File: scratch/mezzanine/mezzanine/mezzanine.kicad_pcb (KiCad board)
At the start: 2 copper layers, 141.5 x 62.2 mm, 18 parts, among them J101 Conn_02x20_Counter_Clockwise_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, J102 Conn_02x20_Counter_Clockwise_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, J103 Conn_02x10_Odd_Even, U101 Caravel_COB, U102 Caravel_COB

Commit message: padring v0.1
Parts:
- added G***: LOGO, Symbol:waferspace_pin1, F.Cu at (207.7, 123.9)
- added G***: LOGO, Symbol:waferspace_pin1, F.Cu at (208.1, 142.3)
- added G***: LOGO, Symbol:waferspace_pin1, B.Cu at (225.1, 155.1)
- added U101: Caravel_COB, WafeSpace:waferspace_default_padring_v0, F.Cu at (214.1, 148.5)
- added U101: Caravel_COB, WafeSpace:waferspace_default_padring_v0, B.Cu at (231.5, 148.3)
- added U102: Caravel_COB, WafeSpace:caravel_gfmpw_1_0_asap, F.Cu at (153.4, 133.3)
- added U103: Caravel_COB, WafeSpace:LGA2, B.Cu at (153.4, 140.0)
- added U104: Caravel_COB, WafeSpace:LGA1, F.Cu at (231.6, 148.4)
- added U104: Caravel_COB, WafeSpace:LGA1, B.Cu at (214.2, 148.4)
- renumbered U101 to U102, U102 to U104
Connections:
- U104 pad 1: (no net) -> unconnected-(U104-mprj_io[24]-Pad1) (x2)
- U104 pad 2: (no net) -> unconnected-(U104-mprj_io[25]-Pad2) (x2)
- U104 pad 3: (no net) -> unconnected-(U104-mprj_io[26]-Pad3) (x2)
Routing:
- net (no net): track 0.00 -> 5.02 mm, vias 2 -> 5
- net unconnected-(U102-mprj_io[23]-Pad45): track 0.00 -> 3.72 mm, vias 0 -> 1
- net unconnected-(U102-mprj_io[0]_JTAG-Pad22): track 0.00 -> 2.00 mm, vias 0 -> 1
- net unconnected-(U102-mprj_io[1]_SDO-Pad23): track 0.00 -> 1.84 mm, vias 0 -> 1
- net unconnected-(U102-mprj_io[2]_SDI-Pad24): track 0.00 -> 1.64 mm, vias 0 -> 1
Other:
- board size 141.5 x 62.2 mm -> 141.5 x 80 mm

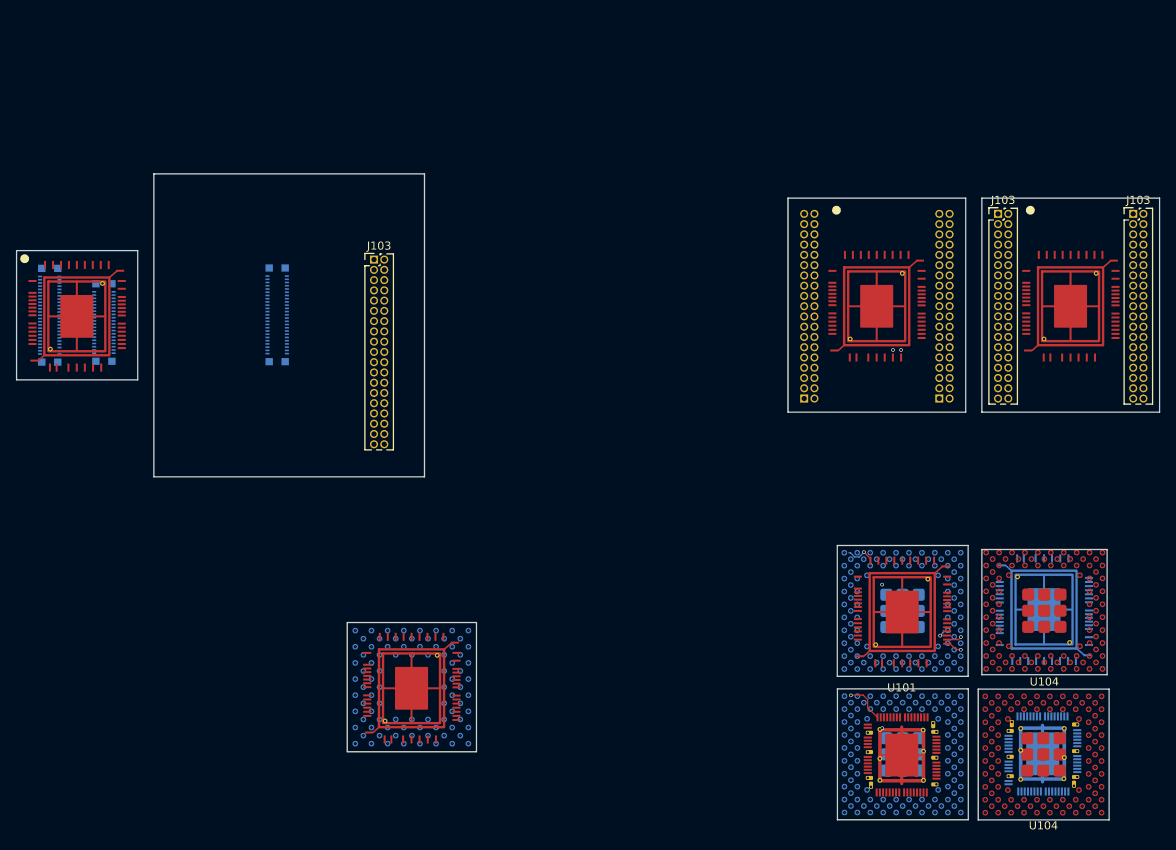
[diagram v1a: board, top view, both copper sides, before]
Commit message: 70pin mezzanine added
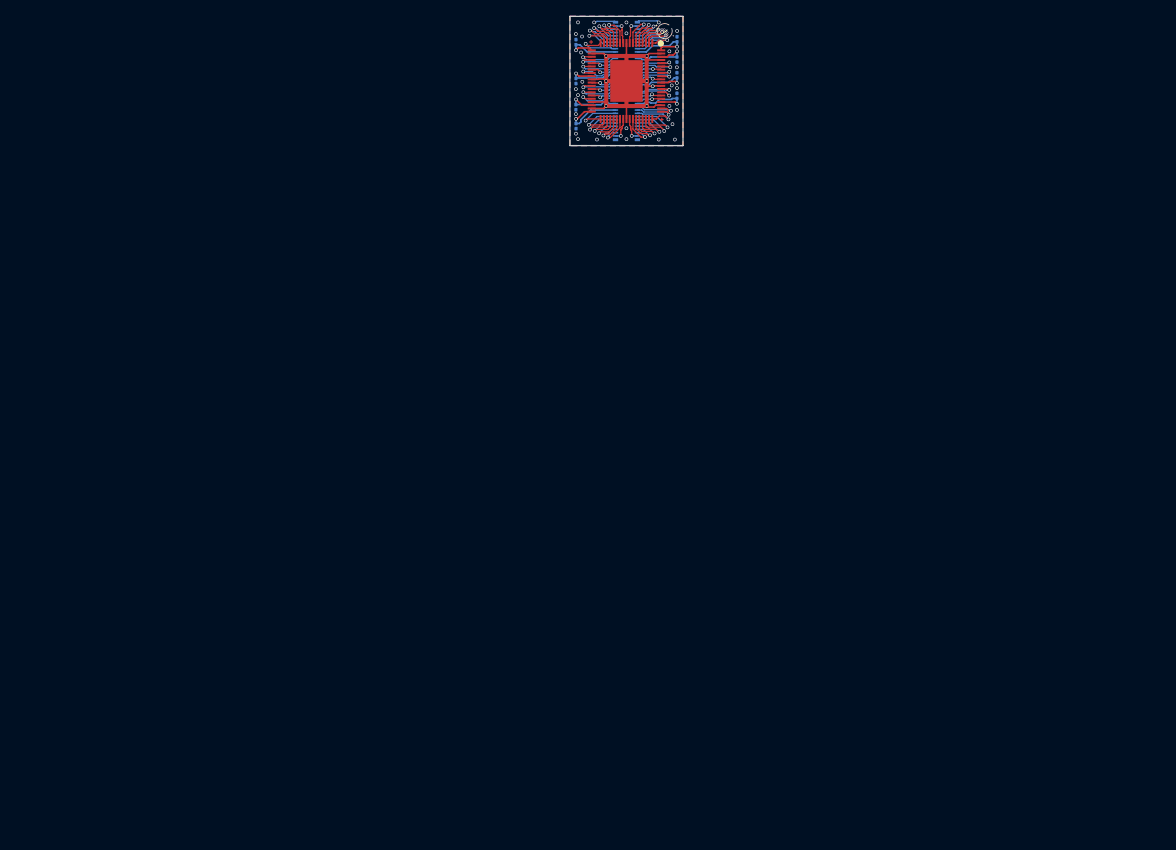
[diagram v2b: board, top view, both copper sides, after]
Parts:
- removed the G*** at (207.7, 123.9)
- removed the G*** at (208.1, 142.3)
- removed the G*** at (225.1, 155.1)
- removed the G*** at (112.7, 88.6)
- removed the G*** at (235.0, 87.4)
- removed the G*** at (211.0, 87.4)
- removed the J101 at (108.6, 94.0)
- removed the J101 at (136.8, 94.0)
- removed J103 (x5): Conn_02x10_Odd_Even, Connector_PinHeader_1.27mm:PinHeader_2x19_P1.27mm_Vertical
- removed U101 (x2): Caravel_COB, WafeSpace:waferspace_default_padring_v0
- removed U102 (x6): Caravel_COB, WafeSpace:caravel_gfmpw_1_0_asap
- removed U103: Caravel_COB, WafeSpace:LGA2
- removed U104 (x4): Caravel_COB, WafeSpace:LGA1
- added C101: C_Small, Capacitor_SMD:C_0201_0603Metric, B.Cu at (173.8, 70.6)
- added C102: C_Small, Capacitor_SMD:C_0201_0603Metric, B.Cu at (186.3, 59.8)
- added C103: C_Small, Capacitor_SMD:C_0201_0603Metric, B.Cu at (173.7, 68.2)
- added C104: C_Small, Capacitor_SMD:C_0201_0603Metric, B.Cu at (186.2, 62.3)
- added C105: C_Small, Capacitor_SMD:C_0201_0603Metric, B.Cu at (173.8, 65.0)
- added C106: C_Small, Capacitor_SMD:C_0201_0603Metric, B.Cu at (186.2, 64.3)
- added C107: C_Small, Capacitor_SMD:C_0201_0603Metric, B.Cu at (173.8, 60.2)
- added C108: C_Small, Capacitor_SMD:C_0201_0603Metric, B.Cu at (186.2, 66.8)
- added G***: LOGO, Symbol:waferspace_pin1_silk, F.Cu at (184.8, 58.7)
- added J101: Conn_02x35_Counter_Clockwise_MountingPin, Connector_Mezzanine:CONN-SMD_70P-P0.40_HCTL_HC-PBB40C-70DP-0.4V-02, B.Cu at (180.0, 65.0)
- J102: value Conn_02x20_Counter_Clockwise_MountingPin -> Conn_2Rows-76Pins; footprint Connector_Mezzanine:CONN-SMD_YXT-BB10-40S-02 -> WafeSpace:waferspace_default_padring_v0.2; moved to F.Cu
- moved J102 71.3 mm to (180.0, 65.0), turned to 180 degrees
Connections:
- J102 pad 1: unconnected-(J102-Pin_1-Pad1) -> /PIN 63
- J102 pad 10: unconnected-(J102-Pin_10-Pad10) -> /PIN 1
- J102 pad 11: unconnected-(J102-Pin_11-Pad11) -> /PIN 2
- J102 pad 12: unconnected-(J102-Pin_12-Pad12) -> /PIN 3
- J102 pad 13: unconnected-(J102-Pin_13-Pad13) -> /PIN 4
- J102 pad 14: unconnected-(J102-Pin_14-Pad14) -> /PIN 5
- J102 pad 15: unconnected-(J102-Pin_15-Pad15) -> /PIN 6
- J102 pad 16: unconnected-(J102-Pin_16-Pad16) -> /PIN 7
- J102 pad 17: unconnected-(J102-Pin_17-Pad17) -> /PIN 8
- J102 pad 18: unconnected-(J102-Pin_18-Pad18) -> /PIN 9
- J102 pad 19: unconnected-(J102-Pin_19-Pad19) -> GND
- J102 pad 2: unconnected-(J102-Pin_2-Pad2) -> /PIN 64
- J102 pad 20: unconnected-(J102-Pin_20-Pad20) -> /PIN 10
- J102 pad 21: unconnected-(J102-Pin_21-Pad21) -> /PIN 11
- J102 pad 22: unconnected-(J102-Pin_22-Pad22) -> /PIN 12
- J102 pad 23: unconnected-(J102-Pin_23-Pad23) -> /PIN 13
- J102 pad 24: unconnected-(J102-Pin_24-Pad24) -> /PIN 14
- J102 pad 25: unconnected-(J102-Pin_25-Pad25) -> /PIN 15
- J102 pad 26: unconnected-(J102-Pin_26-Pad26) -> /PIN 16
- J102 pad 27: unconnected-(J102-Pin_27-Pad27) -> GND
- J102 pad 28: unconnected-(J102-Pin_28-Pad28) -> /PIN 18
- J102 pad 29: unconnected-(J102-Pin_29-Pad29) -> /PIN 19
- J102 pad 3: unconnected-(J102-Pin_3-Pad3) -> /PIN 65
- J102 pad 30: unconnected-(J102-Pin_30-Pad30) -> /PIN 20
- J102 pad 31: unconnected-(J102-Pin_31-Pad31) -> /PIN 21
- J102 pad 32: unconnected-(J102-Pin_32-Pad32) -> /PIN 22
- J102 pad 33: unconnected-(J102-Pin_33-Pad33) -> /PIN 23
- J102 pad 34: unconnected-(J102-Pin_34-Pad34) -> GND
- J102 pad 35: unconnected-(J102-Pin_35-Pad35) -> /PIN 25
- J102 pad 36: unconnected-(J102-Pin_36-Pad36) -> GND
- J102 pad 37: unconnected-(J102-Pin_37-Pad37) -> /PIN 27
- J102 pad 38: unconnected-(J102-Pin_38-Pad38) -> /PIN 28
- J102 pad 39: unconnected-(J102-Pin_39-Pad39) -> /PIN 29
- J102 pad 4: unconnected-(J102-Pin_4-Pad4) -> /PIN 66
- J102 pad 40: unconnected-(J102-Pin_40-Pad40) -> /PIN 30
- J102 pad 5: unconnected-(J102-Pin_5-Pad5) -> /PIN 67
- J102 pad 6: unconnected-(J102-Pin_6-Pad6) -> /PIN 68
- J102 pad 7: unconnected-(J102-Pin_7-Pad7) -> /PIN 69
- J102 pad 8: unconnected-(J102-Pin_8-Pad8) -> /PIN 70
- J102 pad 9: unconnected-(J102-Pin_9-Pad9) -> GND
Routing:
- net GND: track 0.00 -> 57.3 mm, vias 0 -> 28
- net /PIN 27: track 0.00 -> 8.62 mm, vias 0 -> 1
- net /PIN 62: track 0.00 -> 8.32 mm, vias 0 -> 1
- net /PIN 9: track 0.00 -> 8.14 mm, vias 0 -> 1
- net /PIN 60: track 0.00 -> 8.05 mm, vias 0 -> 1
- net /PIN 25: track 0.00 -> 8.04 mm, vias 0 -> 1
- net /PIN 52: track 0.00 -> 7.97 mm, vias 0 -> 1
- net /PIN 46: track 0.00 -> 7.92 mm, vias 0 -> 1
- net /PIN 16: track 0.00 -> 7.78 mm, vias 0 -> 1
- net /PIN 41: track 0.00 -> 7.44 mm, vias 0 -> 1
- net /PIN 42: track 0.00 -> 7.40 mm, vias 0 -> 1
- net /PIN 6: track 0.00 -> 6.97 mm, vias 0 -> 1
- net /PIN 30: track 0.00 -> 6.91 mm, vias 0 -> 1
- net /PIN 64: track 0.00 -> 6.84 mm, vias 0 -> 1
- net /PIN 65: track 0.00 -> 6.73 mm, vias 0 -> 1
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- added copper zone on B.Cu, net GND
- added copper zone on F.Cu, net GND
- added copper zone on In1.Cu, net GND
- added copper zone on In2.Cu, net GND
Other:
- board size 141.5 x 80 mm -> 14 x 16 mm
- copper layers 2 -> 4
- board text added: "70 PIN MEZZANINE 74 PIN PADRING VERSION: TT01"
- board text added: "Allocated Space For Passives"
- board text removed: "Wave Solderable"

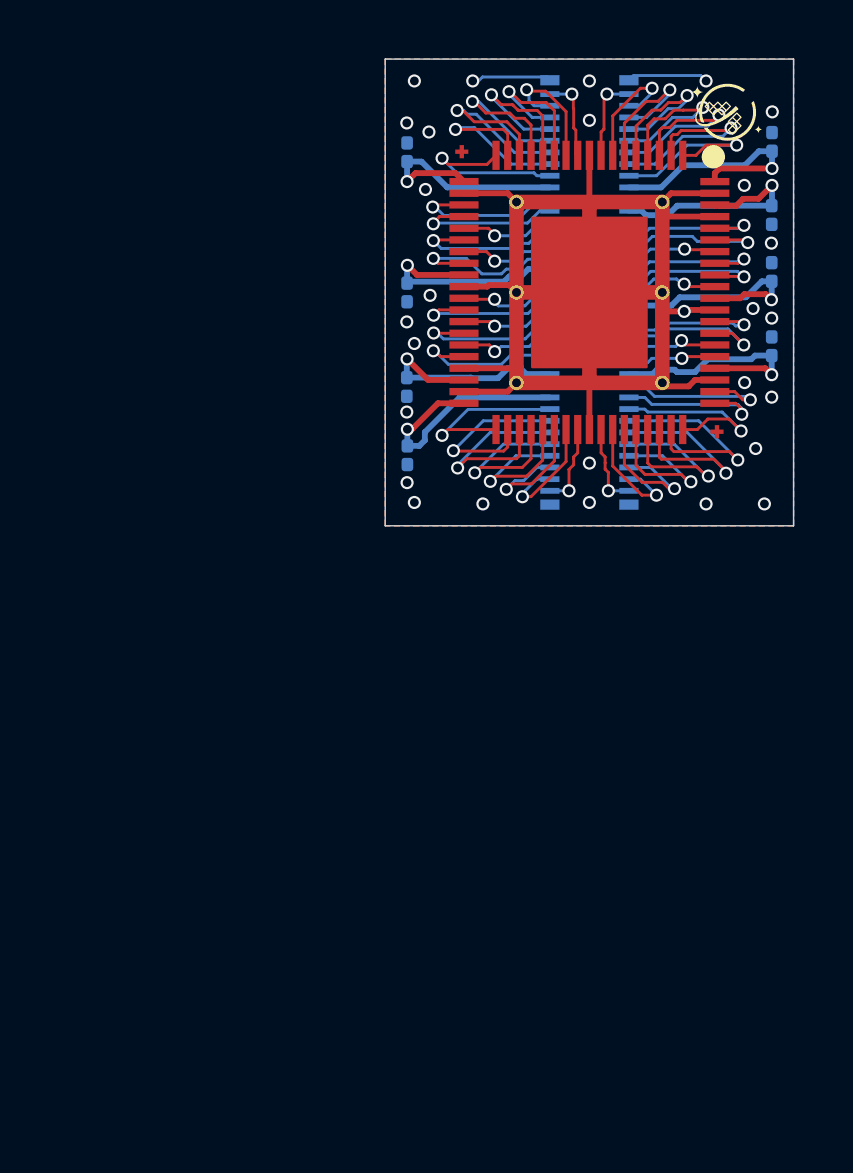
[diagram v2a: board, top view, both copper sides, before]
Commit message: create more pretty symbols for mezzanine and padring
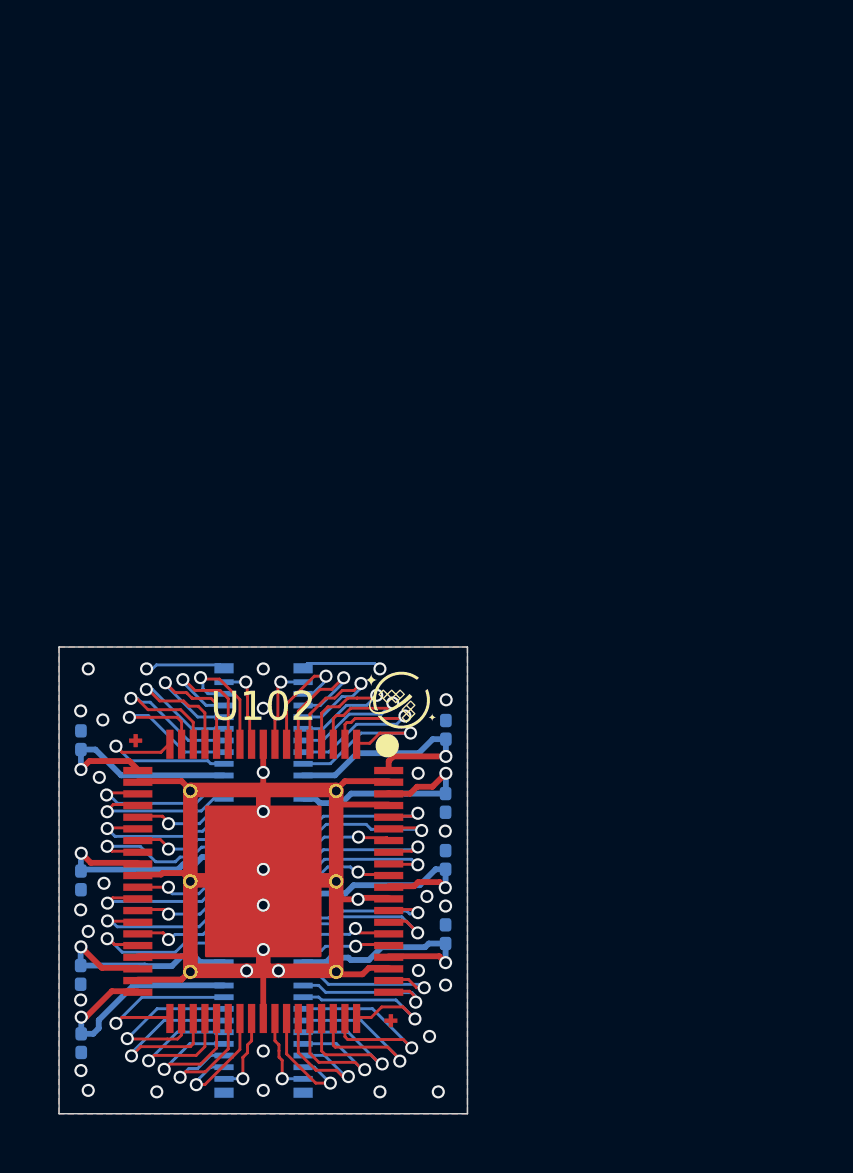
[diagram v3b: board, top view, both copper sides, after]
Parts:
- removed J101: Conn_02x35_Counter_Clockwise_MountingPin, Connector_Mezzanine:CONN-SMD_70P-P0.40_HCTL_HC-PBB40C-70DP-0.4V-02
- removed J102: Conn_2Rows-76Pins, WafeSpace:waferspace_default_padring_v0.2
- added U101: ~, Connector_Mezzanine:CONN-SMD_70P-P0.40_HCTL_HC-PBB40C-70DP-0.4V-02, B.Cu at (168.8, 85.2)
- added U102: ~, WaferSpace:waferspace_default_padring_v0.2, F.Cu at (168.8, 85.2)
- moved C103 23.0 mm to (162.6, 88.4)
- moved C104 23.0 mm to (175.1, 82.5)
- moved C105 23.0 mm to (162.6, 85.2)
- moved C106 23.0 mm to (175.1, 84.5)
- moved C108 23.0 mm to (175.1, 87.0)
- moved C107 23.0 mm to (162.6, 80.3)
- moved C101 23.0 mm to (162.6, 90.7)
- moved C102 23.0 mm to (175.1, 80.0)
- moved G*** 23.0 mm to (173.6, 78.8)
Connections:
- C101 pad 1: /PIN 27 -> VDD_IO_1
- C102 pad 1: /PIN 62 -> VDD_IO_3
- C103 pad 1: /PIN 25 -> VDD_CORE_0
- C104 pad 1: /PIN 60 -> VDD_CORE_1
- C105 pad 1: /PIN 16 -> PWR_AUX_0
- C106 pad 1: /PIN 52 -> PWR_AUX_1
- C107 pad 1: /PIN 9 -> VDD_IO_0
- C108 pad 1: /PIN 46 -> VDD_IO_2
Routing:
- net /PIN 27: track 8.62 -> 0.00 mm, vias 1 -> 0
- net VDD_IO_1: track 0.00 -> 8.62 mm, vias 0 -> 1
- net VDD_IO_3: track 0.00 -> 8.32 mm, vias 0 -> 1
- net /PIN 62: track 8.32 -> 0.00 mm, vias 1 -> 0
- net VDD_IO_0: track 0.00 -> 8.14 mm, vias 0 -> 1
- net /PIN 9: track 8.14 -> 0.00 mm, vias 1 -> 0
- net VDD_CORE_1: track 0.00 -> 8.05 mm, vias 0 -> 1
- net /PIN 60: track 8.05 -> 0.00 mm, vias 1 -> 0
- net VDD_CORE_0: track 0.00 -> 8.04 mm, vias 0 -> 1
- net /PIN 25: track 8.04 -> 0.00 mm, vias 1 -> 0
- net /PIN 52: track 7.97 -> 0.00 mm, vias 1 -> 0
- net PWR_AUX_1: track 0.00 -> 7.97 mm, vias 0 -> 1
- net /PIN 46: track 7.92 -> 0.00 mm, vias 1 -> 0
- net VDD_IO_2: track 0.00 -> 7.92 mm, vias 0 -> 1
- net PWR_AUX_0: track 0.00 -> 7.78 mm, vias 0 -> 1
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
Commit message: housekeeping
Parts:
- moved C106 0.63 mm to (175.1, 85.1), turned to -90 degrees
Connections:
- U101 pad 12: GND -> /pad_69
- U101 pad 13: /pad_69 -> /pad_68
- U101 pad 14: /pad_68 -> /pad_67
- U101 pad 15: /pad_67 -> /pad_66
- U101 pad 16: /pad_66 -> /pad_65
- U101 pad 17: /pad_65 -> /pad_64
- U101 pad 18: /pad_64 -> GND
- U101 pad 20: GND -> /pad_61
- U101 pad 21: /pad_61 -> /pad_60
- U101 pad 22: /pad_60 -> /pad_59
- U101 pad 23: /pad_59 -> /pad_58
- U101 pad 24: /pad_58 -> VDD_IO_2
- U101 pad 25: VDD_IO_2 -> GND
- U101 pad 47: GND -> /pad_32
- U101 pad 48: /pad_32 -> /pad_31
- U101 pad 49: /pad_31 -> /pad_30
- U101 pad 50: /pad_30 -> /pad_29
- U101 pad 51: /pad_29 -> /pad_28
- U101 pad 52: /pad_28 -> /pad_27
- U101 pad 53: /pad_27 -> GND
- U101 pad 54: GND -> PWR_AUX_0
- U101 pad 55: PWR_AUX_0 -> /pad_24
- U101 pad 56: /pad_24 -> /pad_23
- U101 pad 57: /pad_23 -> /pad_22
- U101 pad 58: /pad_22 -> /pad_21
- U101 pad 59: /pad_21 -> /pad_20
- U101 pad 60: /pad_20 -> /pad_19
- U101 pad 61: /pad_19 -> GND
- U101 pad 63: /pad_17 -> /pad_16
- U101 pad 64: /pad_16 -> /pad_15
- U101 pad 65: /pad_15 -> /pad_14
- U101 pad 66: /pad_14 -> /pad_13
- U101 pad 67: /pad_13 -> /pad_12
- U101 pad 68: /pad_12 -> /pad_11
- U101 pad 69: /pad_11 -> /pad_10
- U101 pad 70: /pad_10 -> /pad_9
- U102 pad 10: /pad_10 -> /pad_9
- U102 pad 11: /pad_11 -> /pad_10
- U102 pad 12: /pad_12 -> /pad_11
- U102 pad 13: /pad_13 -> /pad_12
- U102 pad 14: /pad_14 -> /pad_13
- U102 pad 15: /pad_15 -> /pad_14
- U102 pad 16: /pad_16 -> /pad_15
- U102 pad 17: /pad_17 -> /pad_16
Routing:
- net /pad_17: track 6.01 -> 0.00 mm, vias 1 -> 0
- net PWR_AUX_1: track 7.97 -> 4.17 mm, vias 1 -> 0
- net /pad_9: track 0.00 -> 2.94 mm, vias 0 -> 1
- net /pad_64: track 3.24 -> 5.66 mm
- net /pad_65: track 5.39 -> 3.19 mm
- net /pad_10: track 2.94 -> 4.39 mm
- net /pad_11: track 4.39 -> 5.27 mm
- net /pad_12: track 5.27 -> 5.94 mm
- net /pad_68: track 5.35 -> 6.01 mm
- net /pad_13: track 5.94 -> 6.59 mm
- net /pad_15: track 6.97 -> 6.37 mm
- net GND: vias 35 -> 33
